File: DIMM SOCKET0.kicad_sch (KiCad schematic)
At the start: 2 parts, among them J4 DIMM REF

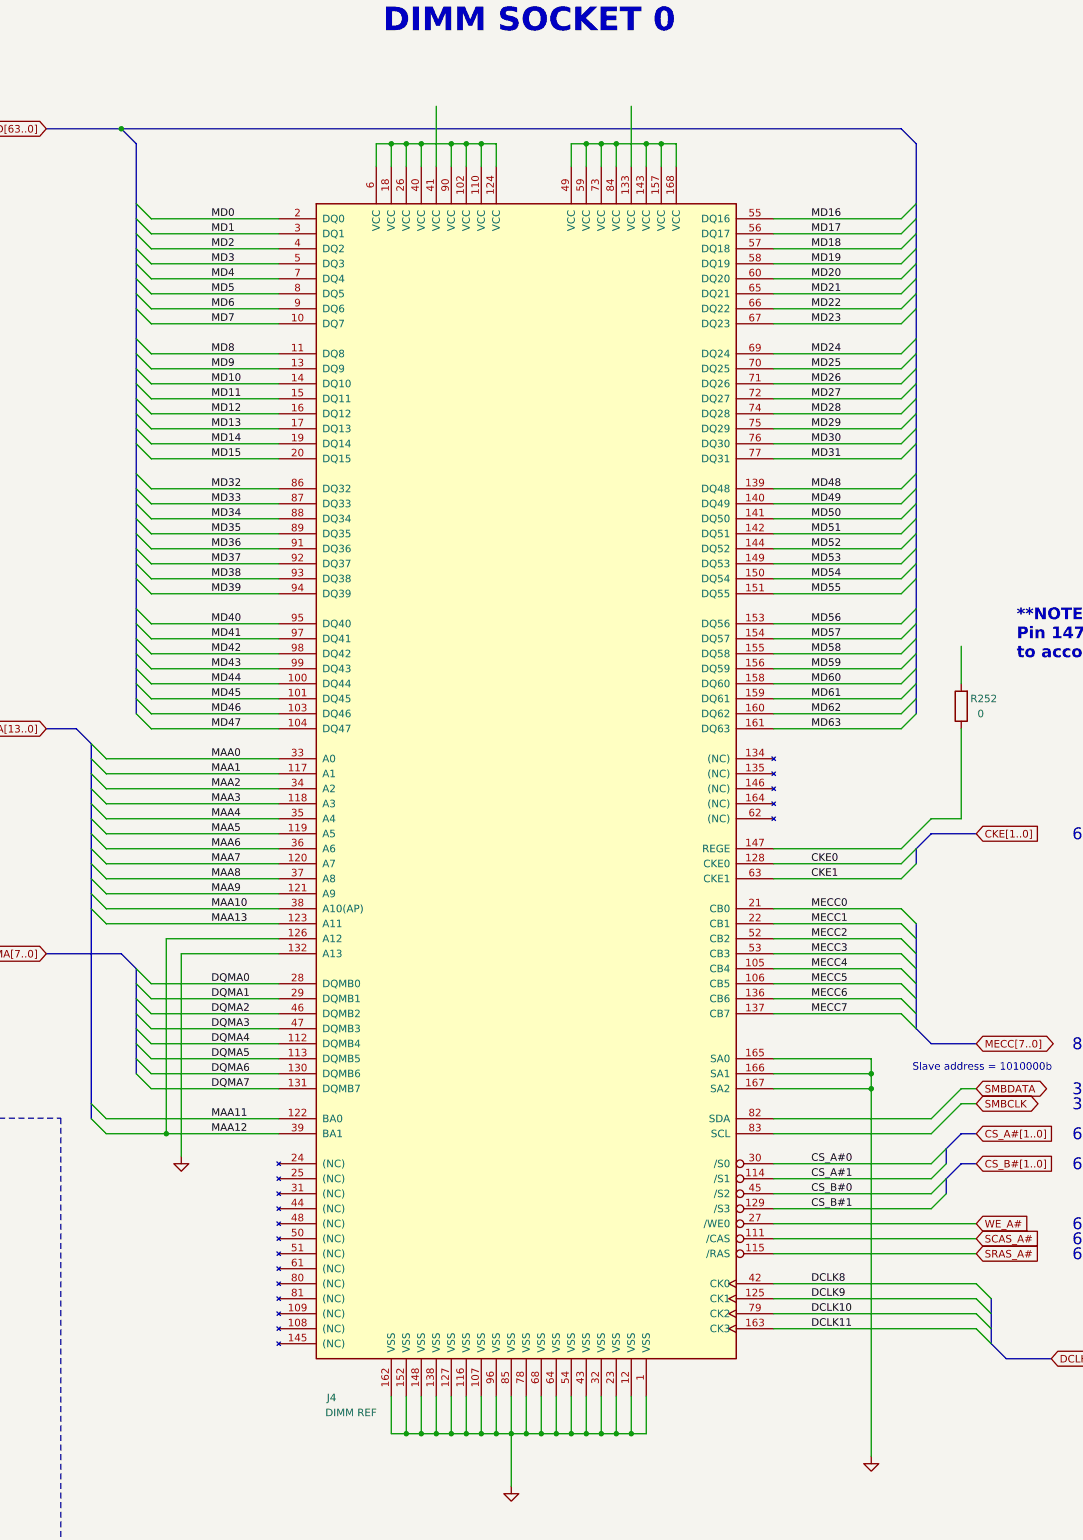
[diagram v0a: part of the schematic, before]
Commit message: page 18 ISA, small fixes
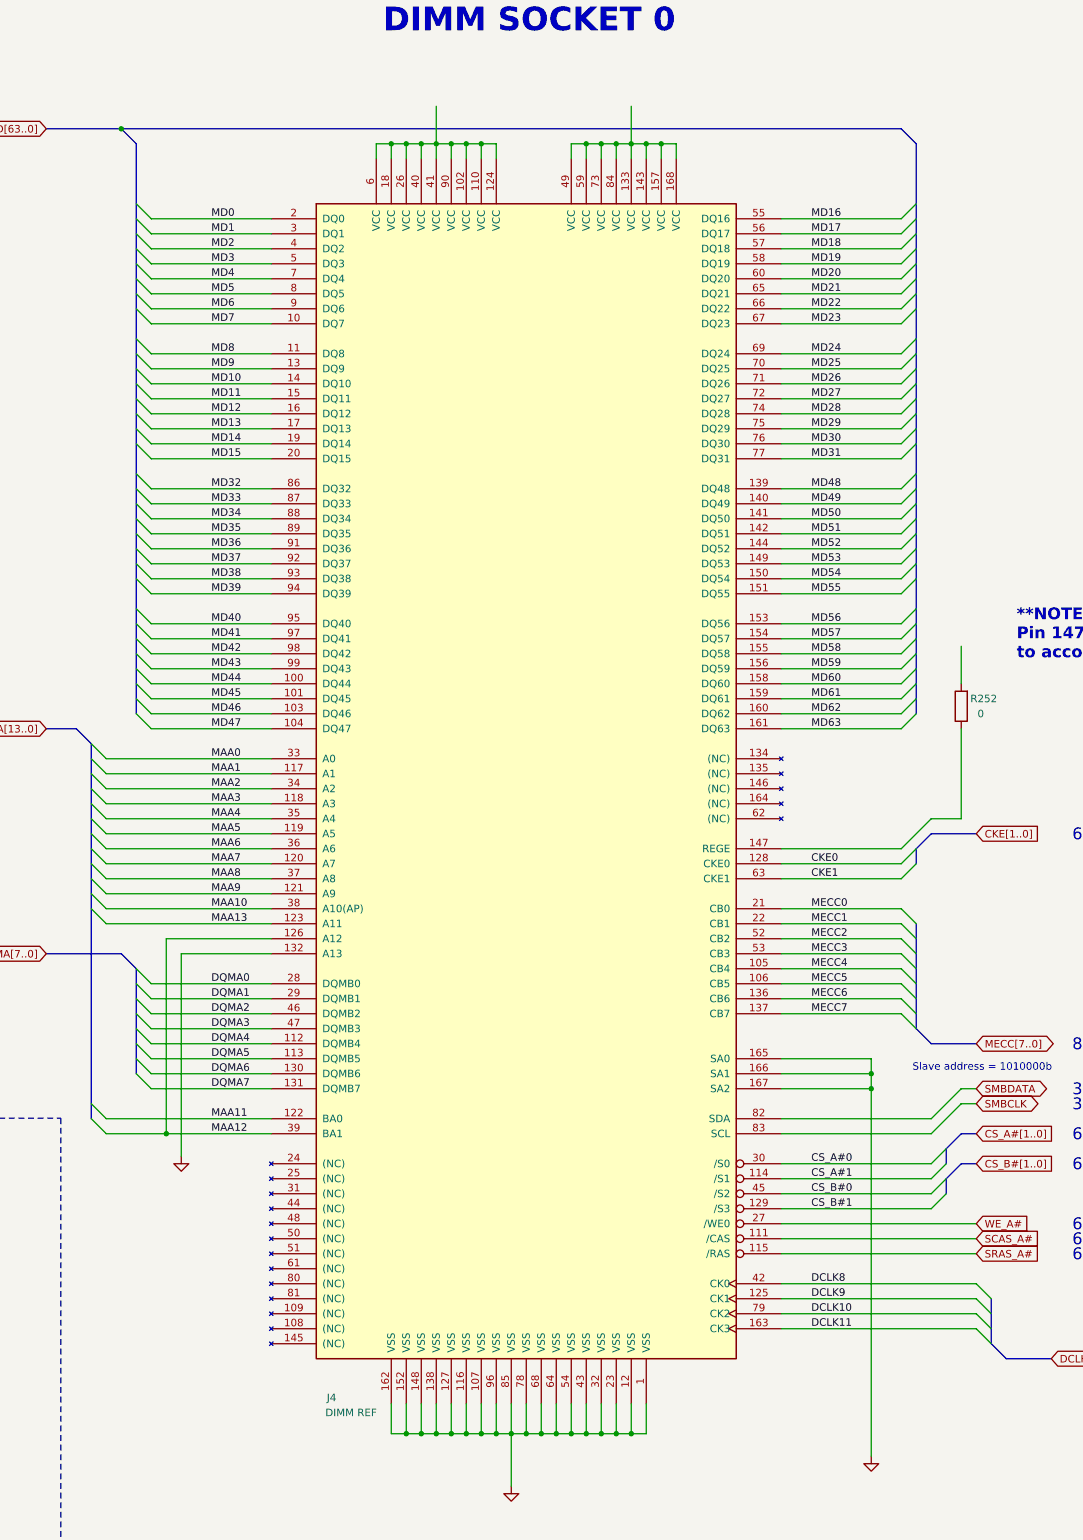
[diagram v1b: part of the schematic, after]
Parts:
- J4: symbol P2-3_era:SDRAM_GENERIC -> P2-3_era:SDRAM_Slot
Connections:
- net at J4.102 (VCC), J4.110 (VCC), J4.124 (VCC)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: now also J4.41 (VCC)
- net at J4.133 (VCC): now also J4.143 (VCC), J4.157 (VCC), J4.168 (VCC), J4.49 (VCC), J4.59 (VCC), J4.73 (VCC), J4.84 (VCC)

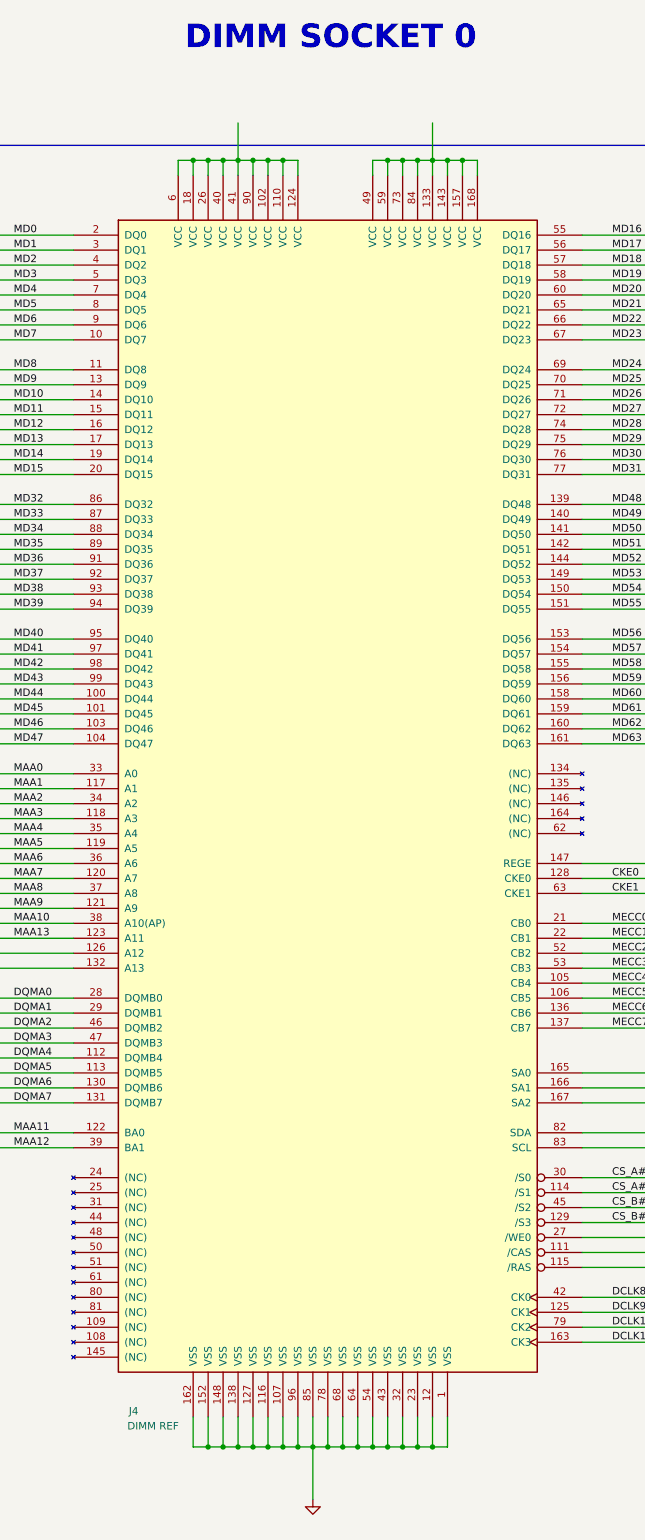
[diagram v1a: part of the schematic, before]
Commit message: page 6,7,8 82443BX chipset, various small fixes
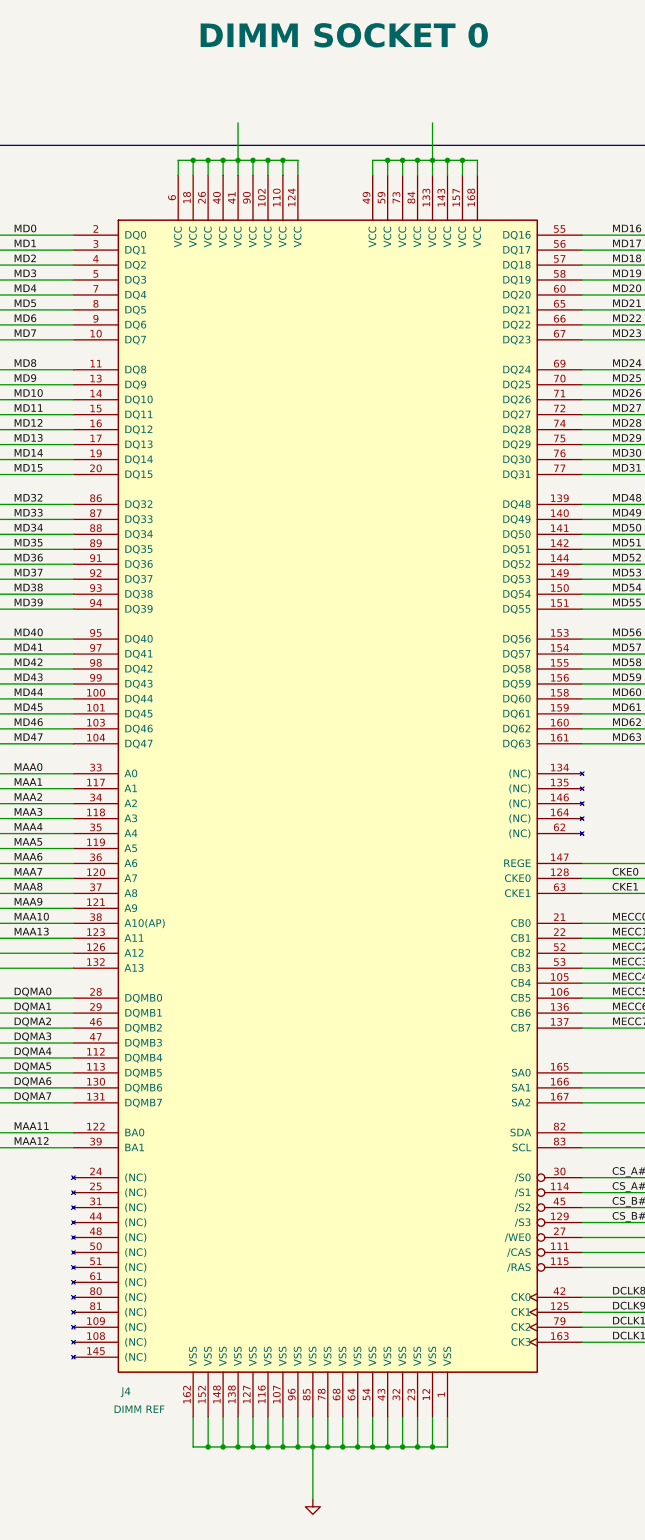
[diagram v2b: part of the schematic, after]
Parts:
- J4: value DIMM REF -> DIMM SOCKET 0
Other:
- note removed: "DIMM SOCKET 0"
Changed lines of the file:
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@@
 			(width 0)
 			(type solid)
-			(color 0 0 0 1)
 		)
 		(fill
@@
 			(width 0)
 			(type solid)
-			(color 0 0 0 1)
 		)
 		(fill
@@
 			(width 0)
 			(type solid)
-			(color 0 0 0 1)
 		)
 		(fill
@@
 			(width 0)
 			(type solid)
-			(color 0 0 0 1)
 		)
 		(fill
@@
 			(width 0)
 			(type dash)
-			(color 0 0 0 1)
 		)
 		(fill
@@
 				(thickness 0.4)
 				(bold yes)
-				(color 0 0 0 1)
 			)
 			(justify left)
@@
 				(thickness 0.254)
 				(bold yes)
-				(color 0 0 0 1)
 			)
 		)
@@
 		)
 	)
-	(text "DIMM SOCKET 0"
-		(exclude_from_sim no)
-		(at 218.948 22.352 0)
-		(effects
-			(font
-				(size 4 4)
-				(thickness 0.8)
-				(bold yes)
-				(color 0 0 0 1)
-			)
-		)
-	)
 	(text "10"
 		(exclude_from_sim no)
@@
 		(dnp no)
 		(property "Reference" "J4"
-			(at 184.658 255.524 0)
+			(at 183.388 252.222 0)
 			(effects
 				(font
@@
 			)
 		)
-		(property "Value" "DIMM REF"
-			(at 184.404 258.064 0)
+		(property "Value" "DIMM SOCKET 0"
+			(at 196.342 22.098 0)
 			(effects
 				(font
-					(size 1.27 1.27)
+					(size 4 4)
+					(thickness 0.8)
+					(bold yes)
 				)
 				(justify left)
@@
 			)
 		)
-		(property "Description" "DIMM SOCKET"
-			(at 220.218 179.07 0)
+		(property "Description" "DIMM REF"
+			(at 186.436 255.27 0)
 			(effects
 				(font
 					(size 1.27 1.27)
 				)
-				(hide yes)
 			)
 		)
